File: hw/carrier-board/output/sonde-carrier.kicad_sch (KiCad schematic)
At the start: 16 parts

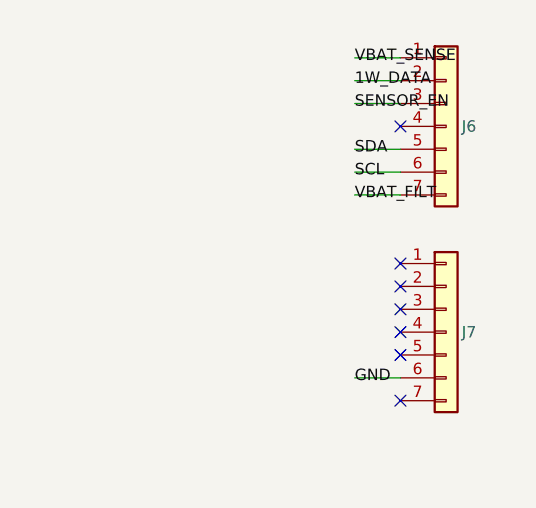
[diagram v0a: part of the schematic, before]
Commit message: feat: hand-routed carrier board PCB — 0 unconnected, 21 DRC (inherent)
Manually routed all 9 signal nets on the sonde carrier board:
- VBAT, VBAT_FILT (0.5mm power traces)
- SENSOR_V (0.3mm power trace)
- SENSOR_EN, SDA, SCL, 1W_DATA, VBAT_SENSE (0.25mm signals)
- GND via B.Cu copper pour with vias

DRC: 21 violations (15 lib_footprint_mismatch + 6 solder_mask_bridge)
ERC: 0 violations
Unconnected: 0

Co-authored-by: Copilot <223556219+Copilot@users.noreply.github.com>
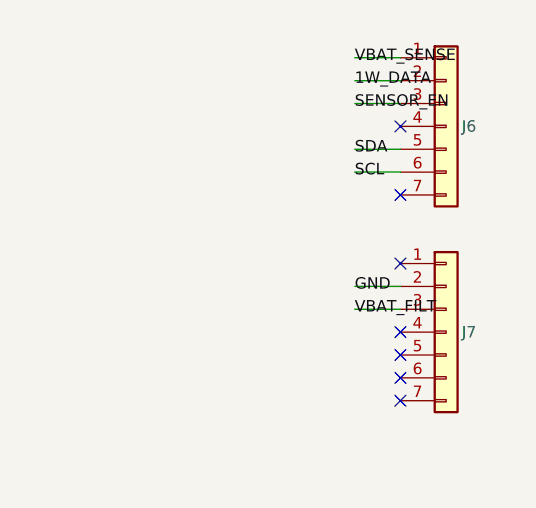
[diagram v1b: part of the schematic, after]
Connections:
- net GND: now also J7.2 (Pin_2); no longer J7.6 (Pin_6)
- net VBAT_FILT: now also J7.3 (Pin_3); no longer J6.7 (Pin_7)
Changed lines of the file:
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@@
   (wire
     (pts
-      (xy 105.41 151.13)
-      (xy 100.33 151.13)
-    )
-    (stroke
-      (width 0)
-      (type default)
-    )
-  )
-  (wire
-    (pts
-      (xy 105.41 171.45)
-      (xy 100.33 171.45)
+      (xy 105.41 161.29)
+      (xy 100.33 161.29)
+    )
+    (stroke
+      (width 0)
+      (type default)
+    )
+  )
+  (wire
+    (pts
+      (xy 105.41 163.83)
+      (xy 100.33 163.83)
     )
     (stroke
@@
   )
   (label
+    "GND"
+    (at 100.33 161.29 0)
+    (effects
+      (font
+        (size 1.27 1.27)
+      )
+    )
+  )
+  (label
     "VBAT_FILT"
-    (at 100.33 151.13 0)
-    (effects
-      (font
-        (size 1.27 1.27)
-      )
-    )
-  )
-  (label
-    "GND"
-    (at 100.33 171.45 0)
+    (at 100.33 163.83 0)
     (effects
       (font
@@
   )
   (no_connect
+    (at 105.41 151.13)
+  )
+  (no_connect
     (at 105.41 158.75)
   )
   (no_connect
-    (at 105.41 161.29)
-  )
-  (no_connect
-    (at 105.41 163.83)
-  )
-  (no_connect
     (at 105.41 166.37)
   )
@@
   )
   (no_connect
+    (at 105.41 171.45)
+  )
+  (no_connect
